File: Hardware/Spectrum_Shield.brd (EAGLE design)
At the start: 59.7 x 53.3 mm, 25 parts, among them IC1 MSGEQ7SOIC, IC2 MSGEQ7SOIC, U1 ARDUINO_R3_SHIELD

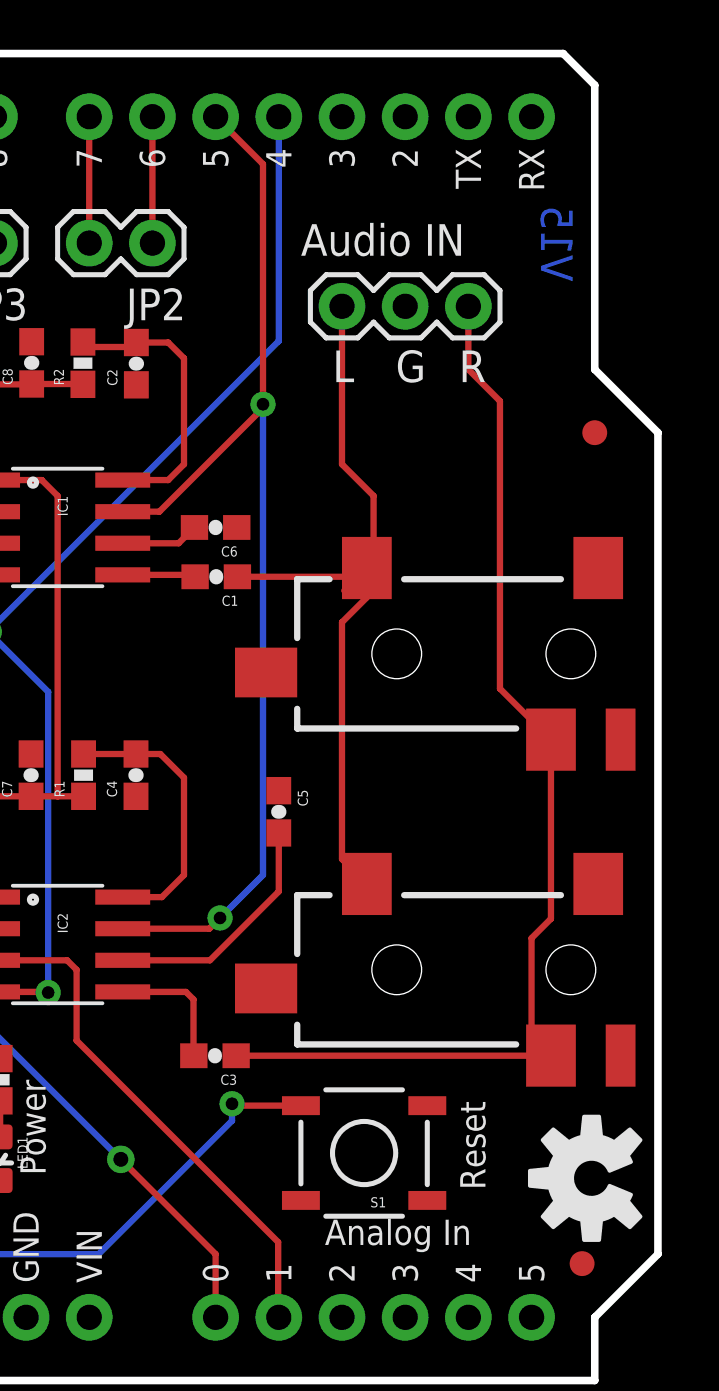
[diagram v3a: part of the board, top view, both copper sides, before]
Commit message: Fixed Sch, Added Input/Output Silk
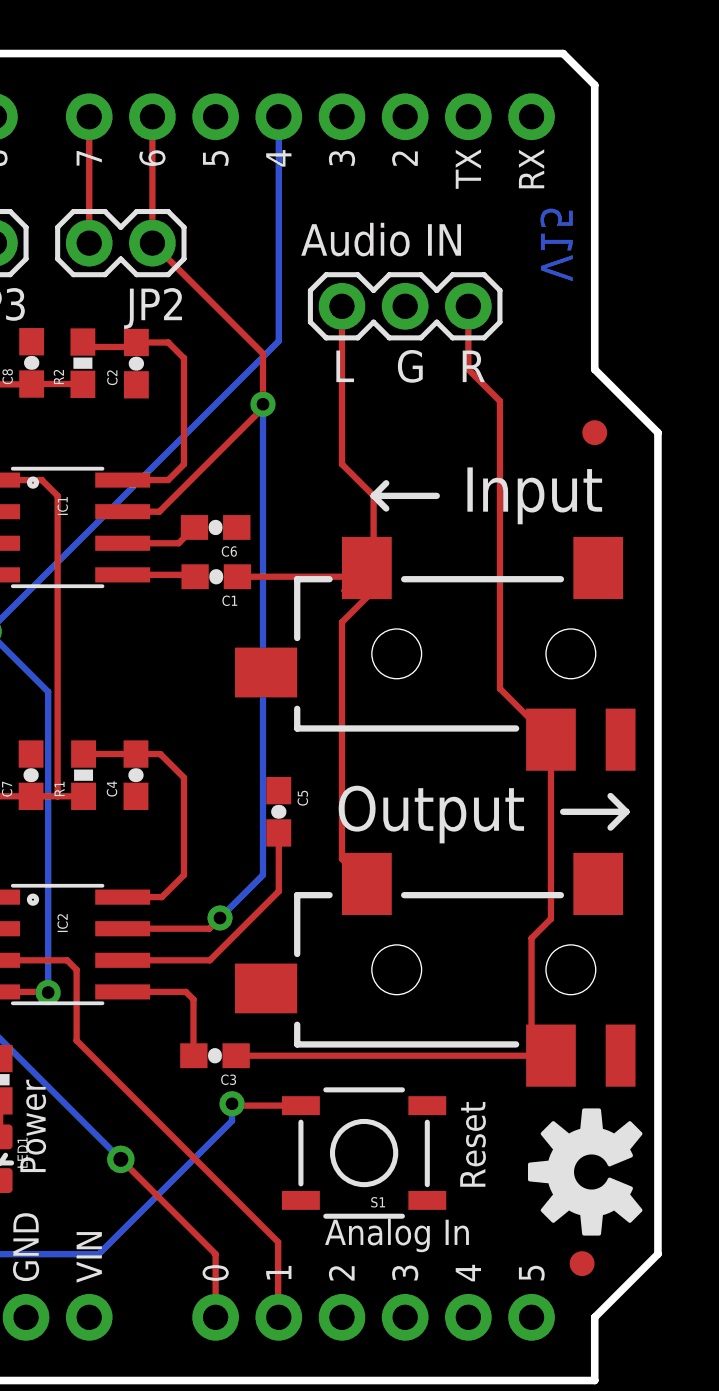
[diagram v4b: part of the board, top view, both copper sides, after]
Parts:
- removed U$1: (no value), SparkFun-Aesthetics:OSHW-LOGO-M
- added FRAME1: FRAME-LETTER, SparkFun-Aesthetics:CREATIVE_COMMONS
- added LOGO1: OSHW-LOGOM, SparkFun-Aesthetics:OSHW-LOGO-M
- added LOGO3: SFE_LOGO_NAME_FLAME.1_INCH, SparkFun-Aesthetics:SFE_LOGO_NAME_FLAME_.1
- LOGO2: value (none) -> SFE_LOGO_FLAME.2_INCH
- renumbered U$2 to LOGO2
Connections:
- removed net N$8: JP2.1, U1.D6
- net RESET: now also JP2.1, U1.D6; no longer U1.D5
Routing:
- net N$8: track 5.08 -> 0.00 mm
- net RESET: track 45.3 -> 46.4 mm
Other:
- board text added: "Input"
- board text added: "J. Lindblom"
- board text added: "Output"
- board text added: "Revised by: P. Alberts"
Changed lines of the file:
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@@
 <layer number="47" name="Measures" color="7" fill="1" visible="no" active="yes"/>
 <layer number="48" name="Document" color="7" fill="1" visible="no" active="yes"/>
-<layer number="49" name="Reference" color="7" fill="1" visible="no" active="yes"/>
+<layer number="49" name="Reference" color="7" fill="1" visible="yes" active="yes"/>
 <layer number="50" name="dxf" color="7" fill="1" visible="no" active="yes"/>
 <layer number="51" name="tDocu" color="6" fill="1" visible="yes" active="yes"/>
@@
 <wire x1="0" y1="50.8" x2="0" y2="2.54" width="0.3048" layer="20"/>
 <wire x1="0" y1="2.54" x2="2.54" y2="0" width="0.3048" layer="20"/>
-<text x="33.274" y="40.386" size="2.1844" layer="22" font="vector" ratio="15" rot="MR270">bliptronics.com</text>
-<text x="35.814" y="36.83" size="1.27" layer="22" font="vector" ratio="15" rot="MR270">Based on design by</text>
+<text x="39.624" y="40.386" size="2.1844" layer="22" font="vector" ratio="15" rot="MR270">bliptronics.com</text>
+<text x="42.164" y="36.83" size="1.27" layer="22" font="vector" ratio="15" rot="MR270">Based on design by</text>
 <text x="45.339" y="45.212" size="1.27" layer="21" font="vector" ratio="15">Audio IN</text>
 <text x="46.609" y="40.132" size="1.27" layer="21" font="vector" ratio="15">L</text>
@@
 <text x="35.0774" y="8.255" size="1.016" layer="21" font="vector" ratio="15" rot="R90">Power</text>
 <text x="56.261" y="47.244" size="1.27" layer="16" font="vector" ratio="15" rot="MR270">V15</text>
+<text x="51.816" y="34.925" size="1.778" layer="21" font="vector" ratio="15">Input</text>
+<wire x1="50.8" y1="35.56" x2="48.514" y2="35.56" width="0.254" layer="21"/>
+<wire x1="48.768" y1="36.068" x2="48.26" y2="35.56" width="0.254" layer="21"/>
+<wire x1="48.26" y1="35.56" x2="48.768" y2="35.052" width="0.254" layer="21"/>
+<text x="46.736" y="22.098" size="1.778" layer="21" font="vector" ratio="15">Output</text>
+<wire x1="55.88" y1="22.86" x2="58.42" y2="22.86" width="0.254" layer="21"/>
+<wire x1="57.785" y1="23.495" x2="58.42" y2="22.86" width="0.254" layer="21"/>
+<wire x1="57.785" y1="22.225" x2="58.42" y2="22.86" width="0.254" layer="21"/>
+<text x="34.671" y="-15.367" size="1.778" layer="51" font="vector" ratio="12">J. Lindblom</text>
+<text x="20.574" y="-17.907" size="1.778" layer="51" font="vector" ratio="12">Revised by: P. Alberts</text>
 </plain>
 <attributes>
@@
 <element name="JP4" library="SparkFun" package="FIDUCIAL-1X2" value="FIDUCIAL1X2" x="56.642" y="4.699"/>
 <element name="JP5" library="SparkFun" package="FIDUCIAL-1X2" value="FIDUCIAL1X2" x="57.15" y="38.1"/>
-<element name="U$1" library="SparkFun-Aesthetics" package="OSHW-LOGO-M" value="" x="57.023" y="8.128" rot="R90"/>
 <element name="AUDIOJACK1" library="SparkFun-Connectors" package="AUDIO-JACK-3.5MM-SMD" value="" x="59.69" y="29.21" rot="R180">
 <attribute name="PROD_ID" value="CONN-10353" x="59.69" y="29.21" size="1.778" layer="27" font="vector" ratio="15" rot="R180" display="off"/>
@@
 <attribute name="PROD_ID" value="CONN-10353" x="59.69" y="16.51" size="1.778" layer="27" font="vector" ratio="15" rot="R180" display="off"/>
 </element>
-<element name="U$2" library="SparkFun-Aesthetics" package="SFE_LOGO_FLAME_.2" value="" x="7.62" y="48.26" rot="R90"/>
+<element name="FRAME1" library="SparkFun-Aesthetics" package="CREATIVE_COMMONS" value="FRAME-LETTER" x="8.89" y="-15.24"/>
+<element name="LOGO1" library="SparkFun-Aesthetics" package="OSHW-LOGO-M" value="OSHW-LOGOM" x="57.023" y="8.382" rot="R90"/>
+<element name="LOGO2" library="SparkFun-Aesthetics" package="SFE_LOGO_FLAME_.2" value="SFE_LOGO_FLAME.2_INCH" x="7.62" y="48.26" rot="R90"/>
+<element name="LOGO3" library="SparkFun-Aesthetics" package="SFE_LOGO_NAME_FLAME_.1" value="SFE_LOGO_NAME_FLAME.1_INCH" x="36.83" y="33.02" rot="MR270"/>
 </elements>
 <signals>
@@
 </signal>
 <signal name="RESET">
-<contactref element="U1" pad="D5"/>
 <contactref element="IC1" pad="7"/>
 <contactref element="IC2" pad="7"/>
-<wire x1="43.815" y1="48.895" x2="41.91" y2="50.8" width="0.254" layer="1"/>
 <via x="43.815" y="39.243" extent="1-16" drill="0.508"/>
 <via x="42.0878" y="18.5928" extent="1-16" drill="0.508"/>
@@
 <wire x1="39.6494" y1="34.925" x2="43.815" y2="39.0906" width="0.254" layer="1"/>
 <wire x1="43.815" y1="39.0906" x2="43.815" y2="39.243" width="0.254" layer="1"/>
-<wire x1="43.815" y1="48.895" x2="43.815" y2="39.243" width="0.254" layer="1"/>
+<contactref element="U1" pad="D6"/>
+<contactref element="JP2" pad="1"/>
+<wire x1="39.37" y1="45.72" x2="39.37" y2="50.8" width="0.254" layer="1"/>
+<wire x1="43.815" y1="39.243" x2="43.815" y2="41.275" width="0.254" layer="1"/>
+<wire x1="43.815" y1="41.275" x2="39.37" y2="45.72" width="0.254" layer="1"/>
 </signal>
 <signal name="STROBE">
@@
 <wire x1="33.2486" y1="9.7924" x2="33.2486" y2="11.2404" width="0.254" layer="1"/>
 </signal>
-<signal name="N$8">
-<contactref element="U1" pad="D6"/>
-<contactref element="JP2" pad="1"/>
-<wire x1="39.37" y1="45.72" x2="39.37" y2="50.8" width="0.254" layer="1"/>
-</signal>
 <signal name="N$9">

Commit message: changed silk
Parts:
- moved LOGO3 12.7 mm to (36.8, 20.3), turned to 90 degrees
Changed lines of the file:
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@@
 <layer number="47" name="Measures" color="7" fill="1" visible="no" active="yes"/>
 <layer number="48" name="Document" color="7" fill="1" visible="no" active="yes"/>
-<layer number="49" name="Reference" color="7" fill="1" visible="yes" active="yes"/>
+<layer number="49" name="Reference" color="7" fill="1" visible="no" active="yes"/>
 <layer number="50" name="dxf" color="7" fill="1" visible="no" active="yes"/>
 <layer number="51" name="tDocu" color="6" fill="1" visible="yes" active="yes"/>
@@
 <wire x1="0" y1="50.8" x2="0" y2="2.54" width="0.3048" layer="20"/>
 <wire x1="0" y1="2.54" x2="2.54" y2="0" width="0.3048" layer="20"/>
-<text x="39.624" y="40.386" size="2.1844" layer="22" font="vector" ratio="15" rot="MR270">bliptronics.com</text>
-<text x="42.164" y="36.83" size="1.27" layer="22" font="vector" ratio="15" rot="MR270">Based on design by</text>
+<text x="32.766" y="14.224" size="2.1844" layer="22" font="vector" ratio="15" rot="MR90">bliptronics.com</text>
+<text x="37.084" y="36.83" size="1.27" layer="22" font="vector" ratio="15" rot="MR270">Based on design by</text>
 <text x="45.339" y="45.212" size="1.27" layer="21" font="vector" ratio="15">Audio IN</text>
 <text x="46.609" y="40.132" size="1.27" layer="21" font="vector" ratio="15">L</text>
@@
 <element name="LOGO1" library="SparkFun-Aesthetics" package="OSHW-LOGO-M" value="OSHW-LOGOM" x="57.023" y="8.382" rot="R90"/>
 <element name="LOGO2" library="SparkFun-Aesthetics" package="SFE_LOGO_FLAME_.2" value="SFE_LOGO_FLAME.2_INCH" x="7.62" y="48.26" rot="R90"/>
-<element name="LOGO3" library="SparkFun-Aesthetics" package="SFE_LOGO_NAME_FLAME_.1" value="SFE_LOGO_NAME_FLAME.1_INCH" x="36.83" y="33.02" rot="MR270"/>
+<element name="LOGO3" library="SparkFun-Aesthetics" package="SFE_LOGO_NAME_FLAME_.1" value="SFE_LOGO_NAME_FLAME.1_INCH" x="36.83" y="20.32" rot="MR90"/>
 </elements>
 <signals>

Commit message: moved fiducials
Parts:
- moved JP4 17.3 mm to (39.4, 5.08)
- moved JP5 1.80 mm to (55.9, 39.4)

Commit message: Fixed Ground Issue
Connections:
- net GND: now also AUDIOJACK1.SLEEVE

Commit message: QC checklist updated, fixed gnd / pin issue
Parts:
- C1, C3: value 1000pF -> 1nF
- IC1, IC2: device SparkFun:SOIC8 -> SparkFun-AnalogIC:SOIC8
- S1: value (none) -> TAC_SWITCHSMD; device SparkFun:TACTILE_SWITCH_SMD -> SparkFun-Retired:TACTILE-SWITCH-SMD
- moved JP5 54.1 mm to (2.54, 48.3)
- renumbered LED1 to D1
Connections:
- new net N$8: JP2.1, U1.D6
- net RESET: now also U1.D5; no longer JP2.1, U1.D6
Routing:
- net N$8: track 0.00 -> 5.08 mm
- net RESET: track 46.4 -> 45.3 mm
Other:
- board text added: "V16"
- board text removed: "V15"
